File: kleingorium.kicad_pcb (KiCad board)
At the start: 2 copper layers, 100 x 100 mm, 93 parts, among them J1 4017 Pins, J10 VCC, J11 GND, J12 4046 Comp In, J13 Select, J14 Input, J15 4046 SigIn, J16 4046 Comp, J17 Output, J18 4046 Comp In, J19 4046 Out, J2 4040 Output, J20 4040 Input, J21 4040 Output, J22 4017 Pins, J23 VCC, J24 GND, J3 4040 Input, J4 4046 Out, J5 4046 Comp, J6 Select, J7 Output, J8 Input, J9 4046 SigIn, Q1 2N3904, Q2 2N3904, Q3 2N3904, Q4 2N3904, Q5 2N3904, Q6 2N3904, SW1 4017 Feedback, SW2 4046 CompIn, SW3 Chain, SW4 4017 Feedback, SW5 4046 CompIn, U1 4046, U12 4040, U13 CD4053B, U14 4017, U15 4046, U2 4017, U3 CD4053B, U4 4040, U5 CD4066BE

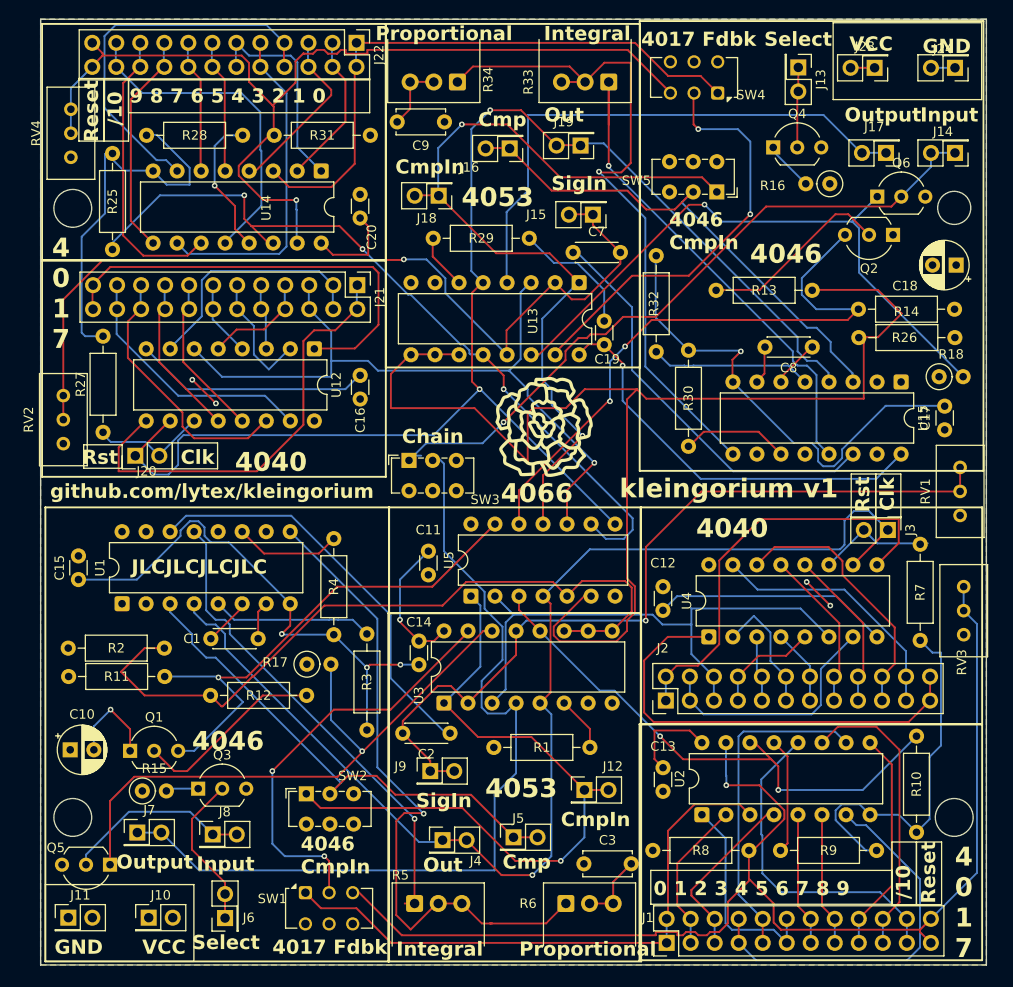
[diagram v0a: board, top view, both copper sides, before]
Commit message: silkscreen adjusments, make RVx text bigger
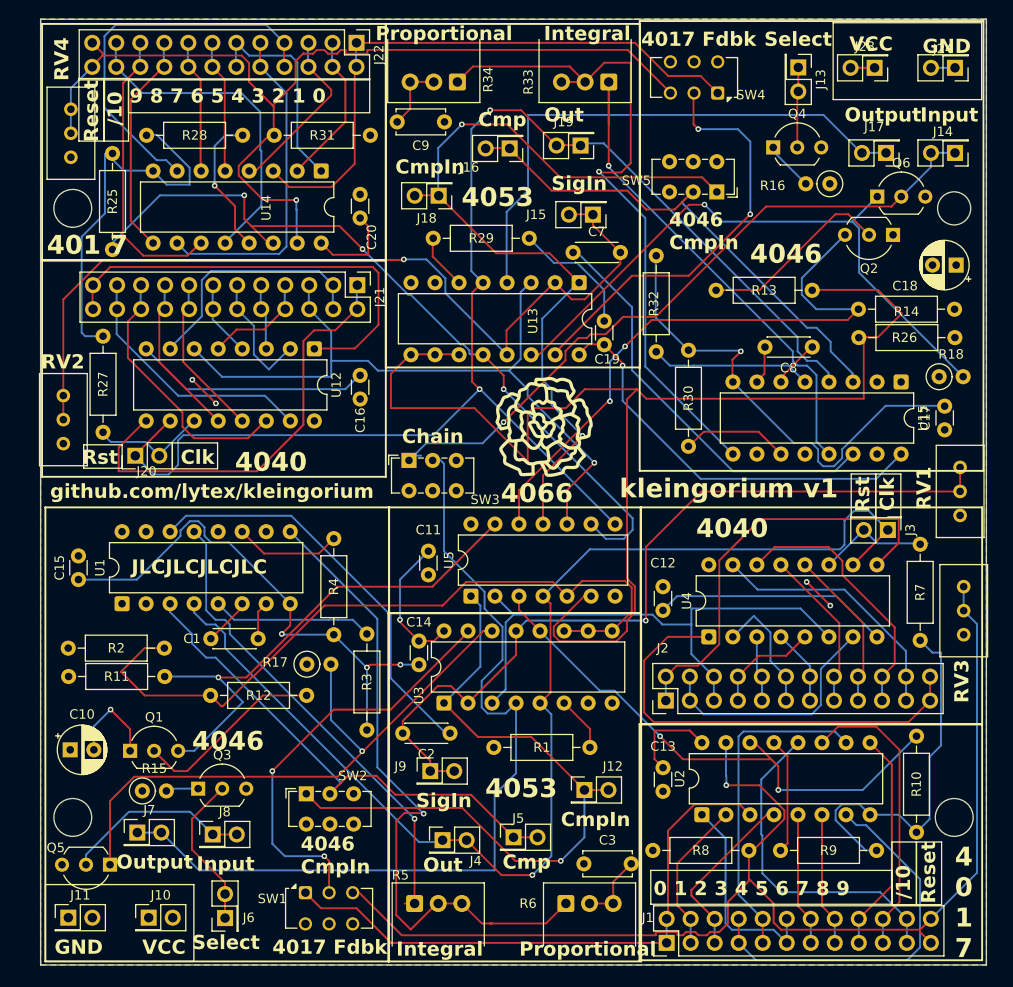
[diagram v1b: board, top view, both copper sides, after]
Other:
- outline, holes or cut-outs redrawn
- board text added: "401 7"
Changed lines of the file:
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@@
 		(tags "Potentiometer vertical Bourns 3296W")
 		(property "Reference" "RV4"
-			(at -2.54 -3.66 90)
+			(at 5.3 -0.96 270)
 			(layer "F.SilkS")
 			(effects
 				(font
-					(size 1 1)
-					(thickness 0.15)
+					(size 1.5 1.5)
+					(thickness 0.3)
+					(bold yes)
 				)
 			)
@@
 		(tags "Potentiometer vertical Bourns 3296W")
 		(property "Reference" "RV1"
-			(at -2.54 -3.66 90)
+			(at -2.21 -3.82 90)
 			(layer "F.SilkS")
 			(effects
 				(font
-					(size 1 1)
-					(thickness 0.15)
+					(size 1.5 1.5)
+					(thickness 0.3)
+					(bold yes)
 				)
 			)
@@
 		(tags "Resistor Axial_DIN0207 series Axial Horizontal pin pitch 10.16mm 0.25W = 1/4W length 6.3mm diameter 2.5mm")
 		(property "Reference" "R27"
-			(at 5.08 -2.37 90)
+			(at 5.08 0 90)
 			(layer "F.SilkS")
 			(effects
@@
 		(tags "Potentiometer vertical Bourns 3296W")
 		(property "Reference" "RV2"
-			(at -2.54 -3.66 90)
+			(at 3.57 -0.05 180)
 			(layer "F.SilkS")
 			(effects
 				(font
-					(size 1 1)
-					(thickness 0.15)
+					(size 1.5 1.5)
+					(thickness 0.3)
+					(bold yes)
 				)
 			)
@@
 		(tags "Potentiometer vertical Bourns 3296W")
 		(property "Reference" "RV3"
-			(at -8 -0.2 90)
+			(at -10 -0.2 90)
 			(layer "F.SilkS")
 			(effects
 				(font
-					(size 1 1)
-					(thickness 0.15)
+					(size 1.5 1.5)
+					(thickness 0.3)
+					(bold yes)
 				)
 			)
@@
 	)
 	(gr_circle
-		(center 183.6 66.95)
-		(end 185.35 66.95)
+		(center 183.59 67)
+		(end 185.34 67)
 		(stroke
 			(width 0.05)
@@
 		)
 	)
-	(gr_text "4\n0\n1\n7"
-		(at 88.2 82 0)
+	(gr_text "401 7"
+		(at 87.65 72.05 0)
 		(layer "F.SilkS")
 		(effects
